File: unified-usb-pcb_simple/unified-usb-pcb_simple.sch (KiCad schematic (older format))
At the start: 11 parts, among them J1 USB_C_Receptacle_USB2.0, J2 USB_Out, U1 SRV05-4

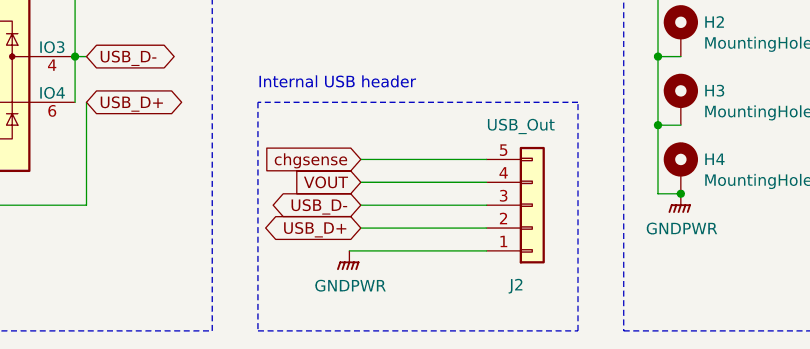
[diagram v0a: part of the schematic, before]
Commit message: added ferrite bead, improved usb track matching
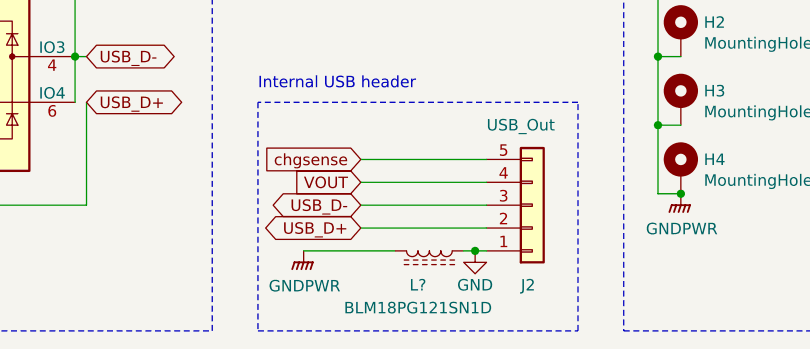
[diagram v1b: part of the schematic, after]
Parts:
- added L?: BLM18PG121SN1D, Inductor_SMD:L_0603_1608Metric, symbol Device:L_Core_Ferrite
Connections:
- net GNDPWR: now also L?.2; no longer J2.1 (Pin_1)
- new net GND: J2.1 (Pin_1), L?.1
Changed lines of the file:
@@
 U 1 1 5E8A3E4C
 P 5350 2300
-F 0 "J2" H 5250 2650 50  0000 L CNN
+F 0 "J2" H 5300 2650 50  0000 L CNN
 F 1 "USB_Out" H 5150 1950 50  0000 L CNN
 F 2 "Connector_JST:JST_SH_SM05B-SRSS-TB_1x05-1MP_P1.00mm_Horizontal" H 5350 2300 50  0001 C CNN
@@
 L power:GNDPWR #PWR03
 U 1 1 5E879D91
-P 4550 2500
-F 0 "#PWR03" H 4550 2300 50  0001 C CNN
-F 1 "GNDPWR" H 4554 2346 50  0000 C CNN
-F 2 "" H 4550 2450 50  0001 C CNN
-F 3 "" H 4550 2450 50  0001 C CNN
-	1    4550 2500
-	1    0    0    -1
-$EndComp
-Wire Wire Line
-	5150 2500 4550 2500
+P 4350 2500
+F 0 "#PWR03" H 4350 2300 50  0001 C CNN
+F 1 "GNDPWR" H 4354 2346 50  0000 C CNN
+F 2 "" H 4350 2450 50  0001 C CNN
+F 3 "" H 4350 2450 50  0001 C CNN
+	1    4350 2500
+	1    0    0    -1
+$EndComp
 Text GLabel 4600 2100 0    50   Input ~ 0
 chgsense
@@
 Wire Wire Line
 	4600 2200 5150 2200
+$Comp
+L Device:L_Core_Ferrite L?
+U 1 1 5E8E3A4F
+P 4900 2500
+F 0 "L?" V 5050 2450 50  0000 C CNN
+F 1 "BLM18PG121SN1D" V 5150 2450 50  0000 C CNN
+F 2 "Inductor_SMD:L_0603_1608Metric" H 4900 2500 50  0001 C CNN
+F 3 "~" H 4900 2500 50  0001 C CNN
+	1    4900 2500
+	0    1    1    0
+$EndComp
+Wire Wire Line
+	5050 2500 5100 2500
+Wire Wire Line
+	4750 2500 4350 2500
+$Comp
+L power:GND #PWR?
+U 1 1 5E8E879D
+P 5100 2500
+F 0 "#PWR?" H 5100 2250 50  0001 C CNN
+F 1 "GND" H 5100 2350 50  0000 C CNN
+F 2 "" H 5100 2500 50  0001 C CNN
+F 3 "" H 5100 2500 50  0001 C CNN
+	1    5100 2500
+	1    0    0    -1
+$EndComp
+Connection ~ 5100 2500
+Wire Wire Line
+	5100 2500 5150 2500
 $EndSCHEMATC

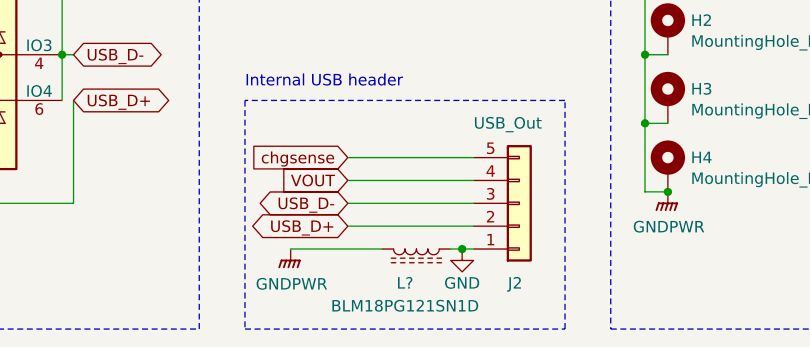
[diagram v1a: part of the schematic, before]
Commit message: added ferrite bead
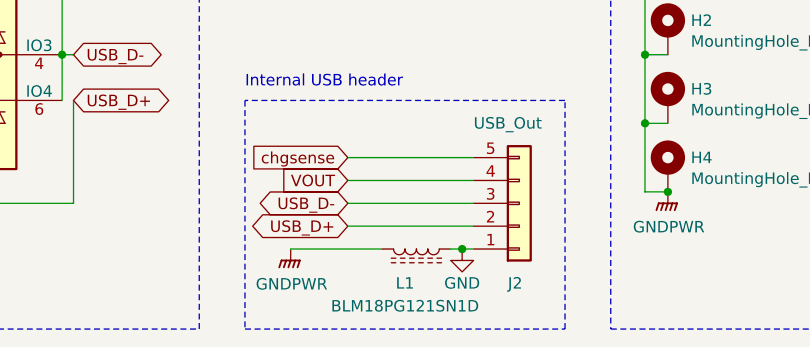
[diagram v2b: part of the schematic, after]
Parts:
- gave numbers to parts that had none: 1
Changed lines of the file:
@@
 	4600 2200 5150 2200
 $Comp
-L Device:L_Core_Ferrite L?
+L Device:L_Core_Ferrite L1
 U 1 1 5E8E3A4F
 P 4900 2500
-F 0 "L?" V 5050 2450 50  0000 C CNN
+F 0 "L1" V 5050 2450 50  0000 C CNN
 F 1 "BLM18PG121SN1D" V 5150 2450 50  0000 C CNN
 F 2 "Inductor_SMD:L_0603_1608Metric" H 4900 2500 50  0001 C CNN
@@
 	4750 2500 4350 2500
 $Comp
-L power:GND #PWR?
+L power:GND #PWR0101
 U 1 1 5E8E879D
 P 5100 2500
-F 0 "#PWR?" H 5100 2250 50  0001 C CNN
+F 0 "#PWR0101" H 5100 2250 50  0001 C CNN
 F 1 "GND" H 5100 2350 50  0000 C CNN
 F 2 "" H 5100 2500 50  0001 C CNN

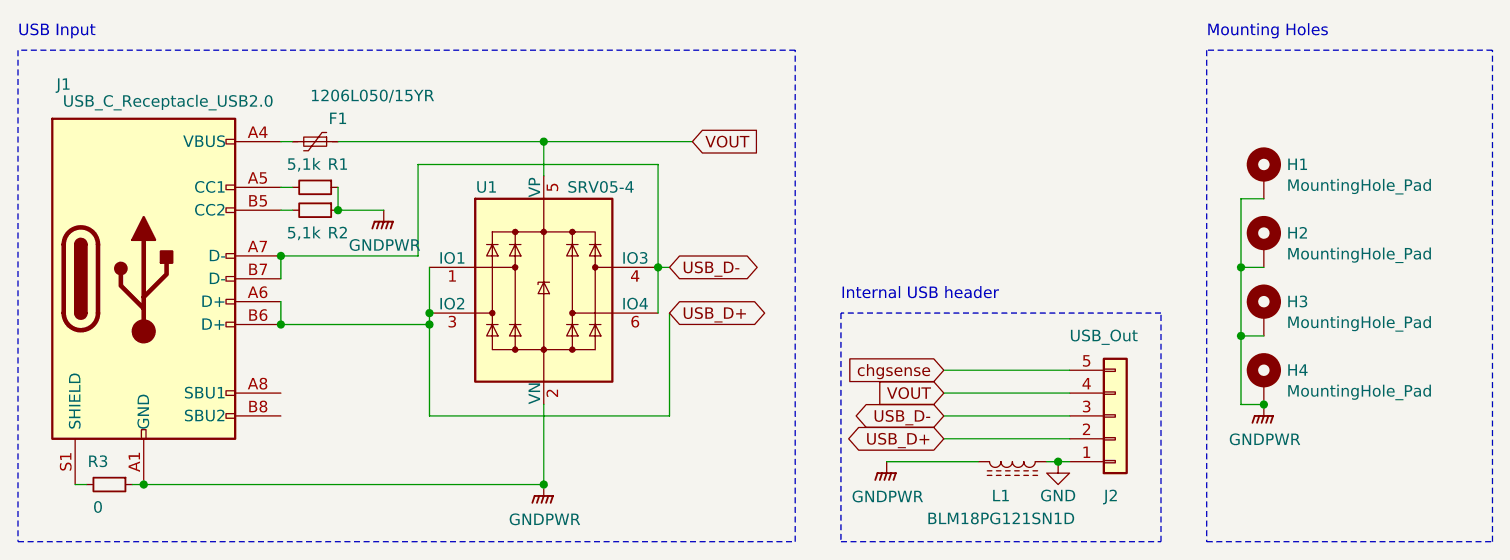
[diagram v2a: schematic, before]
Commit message: created plane for usb-shielding below the connector
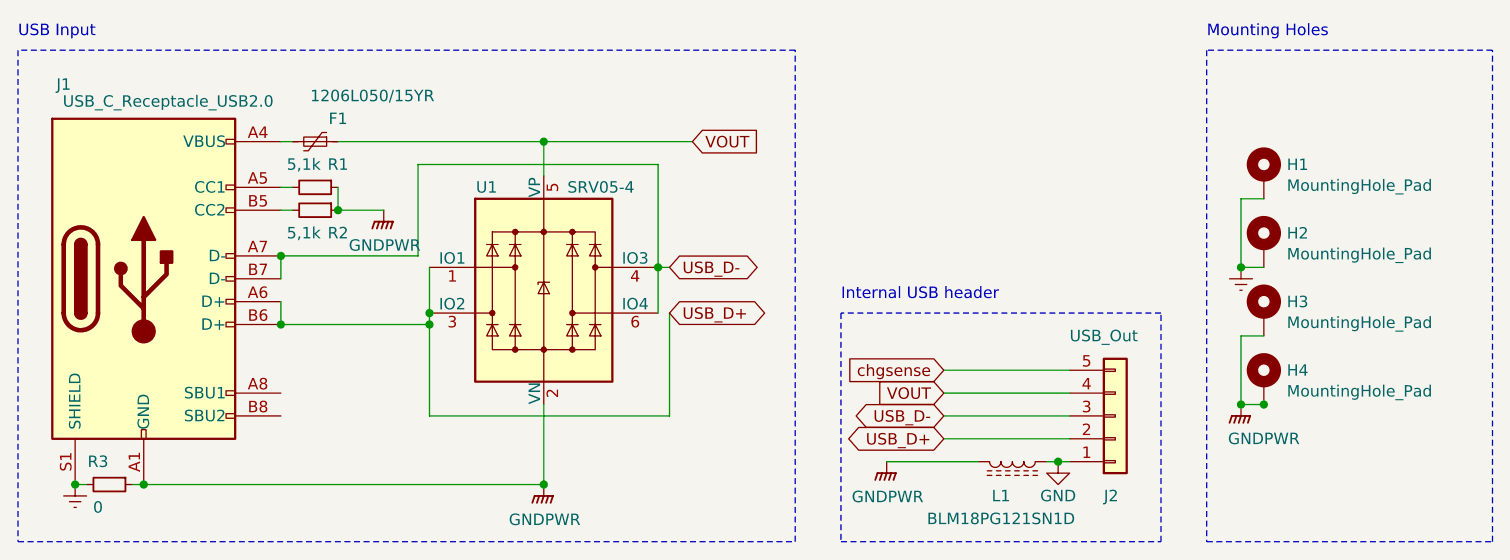
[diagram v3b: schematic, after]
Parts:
- F1: LCSC (none) -> C151162
- H1, H2, H3, H4, J1, J2: LCSC (none) -> /
- L1: LCSC (none) -> C73100
- R1, R2: LCSC (none) -> C23186
- R3: LCSC (none) -> C21189
- U1: LCSC (none) -> C85364
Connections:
- net GNDPWR: no longer H1.1, H2.1
- net Earth: now reaches J1.S1 (SHIELD), R3.2
- net Earth: now also H1.1, H2.1
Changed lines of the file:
@@
 F 2 "Connector_USB:USB_C_Receptacle_HRO_TYPE-C-31-M-12" H 1250 1700 50  0001 C CNN
 F 3 "https://www.usb.org/sites/default/files/documents/usb_type-c.zip" H 1250 1700 50  0001 C CNN
+F 4 "/" H 1100 1700 50  0001 C CNN "LCSC"
 	1    1100 1700
 	1    0    0    -1
@@
 F 2 "Package_TO_SOT_SMD:SOT-23-6" H 3550 1300 50  0001 C CNN
 F 3 "http://www.onsemi.com/pub/Collateral/SRV05-4-D.PDF" H 2850 1750 50  0001 C CNN
+F 4 "C85364" H 2850 1750 50  0001 C CNN "LCSC"
 	1    2850 1750
 	1    0    0    -1
@@
 F 2 "Resistor_SMD:R_0603_1608Metric" H 950 2600 50  0001 C CNN
 F 3 "~" H 950 2600 50  0001 C CNN
+F 4 "C21189" H 950 2600 50  0001 C CNN "LCSC"
 	1    950  2600
 	0    1    1    0
@@
 F 2 "Resistor_SMD:R_0603_1608Metric" H 1850 1300 50  0001 C CNN
 F 3 "~" H 1850 1300 50  0001 C CNN
+F 4 "C23186" H 1850 1300 50  0001 C CNN "LCSC"
 	1    1850 1300
 	0    1    1    0
@@
 F 2 "Resistor_SMD:R_0603_1608Metric" H 1850 1400 50  0001 C CNN
 F 3 "~" H 1850 1400 50  0001 C CNN
+F 4 "C23186" H 1850 1400 50  0001 C CNN "LCSC"
 	1    1850 1400
 	0    1    1    0
@@
 F 2 "Connector_JST:JST_SH_SM05B-SRSS-TB_1x05-1MP_P1.00mm_Horizontal" H 5350 2300 50  0001 C CNN
 F 3 "~" H 5350 2300 50  0001 C CNN
+F 4 "/" H 5350 2300 50  0001 C CNN "LCSC"
 	1    5350 2300
 	1    0    0    1
@@
 F 2 "Fuse:Fuse_1206_3216Metric" H 1900 900 50  0001 L CNN
 F 3 "https://datasheet.lcsc.com/szlcsc/1810252220_Fuzetec-Tech-FSMD050-1206-R_C220147.pdf" H 1850 1100 50  0001 C CNN
+F 4 "C151162" H 1850 1100 50  0001 C CNN "LCSC"
 	1    1850 1100
 	0    1    1    0
@@
 F 2 "MountingHole:MountingHole_2.7mm_M2.5_DIN965_Pad" H 6000 1250 50  0001 C CNN
 F 3 "~" H 6000 1250 50  0001 C CNN
+F 4 "/" H 6000 1250 50  0001 C CNN "LCSC"
 	1    6000 1250
 	1    0    0    -1
@@
 F 2 "MountingHole:MountingHole_2.7mm_M2.5_DIN965_Pad" H 6000 1550 50  0001 C CNN
 F 3 "~" H 6000 1550 50  0001 C CNN
+F 4 "/" H 6000 1550 50  0001 C CNN "LCSC"
 	1    6000 1550
 	1    0    0    -1
@@
 F 2 "MountingHole:MountingHole_2.7mm_M2.5_DIN965_Pad" H 6000 1850 50  0001 C CNN
 F 3 "~" H 6000 1850 50  0001 C CNN
+F 4 "/" H 6000 1850 50  0001 C CNN "LCSC"
 	1    6000 1850
 	1    0    0    -1
@@
 F 2 "MountingHole:MountingHole_2.7mm_M2.5_DIN965_Pad" H 6000 2150 50  0001 C CNN
 F 3 "~" H 6000 2150 50  0001 C CNN
+F 4 "/" H 6000 2150 50  0001 C CNN "LCSC"
 	1    6000 2150
 	1    0    0    -1
@@
 	5900 1650 6000 1650
 Wire Wire Line
-	5900 1650 5900 1950
-Wire Wire Line
 	5900 1950 6000 1950
-Connection ~ 5900 1650
 Wire Wire Line
 	5900 1950 5900 2250
 Wire Wire Line
 	5900 2250 6000 2250
-Connection ~ 5900 1950
 $Comp
 L power:GNDPWR #PWR02
 U 1 1 5E8EB80F
-P 6000 2250
-F 0 "#PWR02" H 6000 2050 50  0001 C CNN
-F 1 "GNDPWR" H 6004 2096 50  0000 C CNN
-F 2 "" H 6000 2200 50  0001 C CNN
-F 3 "" H 6000 2200 50  0001 C CNN
-	1    6000 2250
+P 5900 2250
+F 0 "#PWR02" H 5900 2050 50  0001 C CNN
+F 1 "GNDPWR" H 6000 2100 50  0000 C CNN
+F 2 "" H 5900 2200 50  0001 C CNN
+F 3 "" H 5900 2200 50  0001 C CNN
+	1    5900 2250
 	1    0    0    -1
 $EndComp
@@
 F 2 "Inductor_SMD:L_0603_1608Metric" H 4900 2500 50  0001 C CNN
 F 3 "~" H 4900 2500 50  0001 C CNN
+F 4 "C73100" H 4900 2500 50  0001 C CNN "LCSC"
 	1    4900 2500
 	0    1    1    0
@@
 Wire Wire Line
 	5100 2500 5150 2500
+$Comp
+L power:Earth #PWR?
+U 1 1 5EBED781
+P 800 2600
+F 0 "#PWR?" H 800 2350 50  0001 C CNN
+F 1 "Earth" H 800 2450 50  0001 C CNN
+F 2 "" H 800 2600 50  0001 C CNN
+F 3 "~" H 800 2600 50  0001 C CNN
+	1    800  2600
+	1    0    0    -1
+$EndComp
+Connection ~ 800  2600
+$Comp
+L power:Earth #PWR?
+U 1 1 5EBEE999
+P 5900 1650
+F 0 "#PWR?" H 5900 1400 50  0001 C CNN
+F 1 "Earth" H 5900 1500 50  0001 C CNN
+F 2 "" H 5900 1650 50  0001 C CNN
+F 3 "~" H 5900 1650 50  0001 C CNN
+	1    5900 1650
+	1    0    0    -1
+$EndComp
+Connection ~ 5900 1650
+Connection ~ 5900 2250
 $EndSCHEMATC

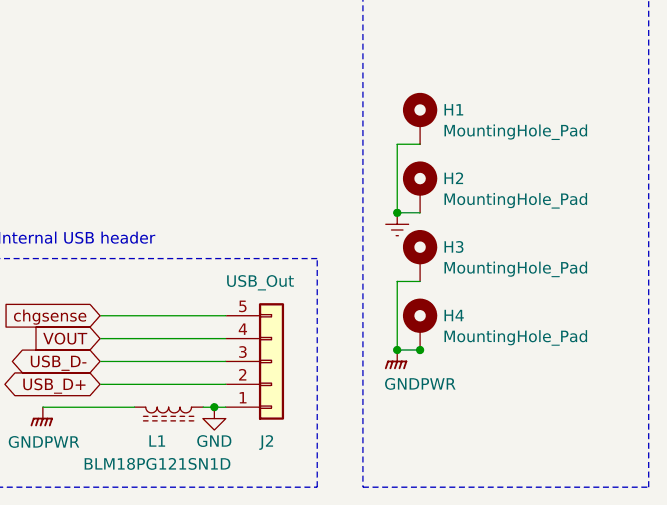
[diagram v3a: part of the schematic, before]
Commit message: resized shield plane
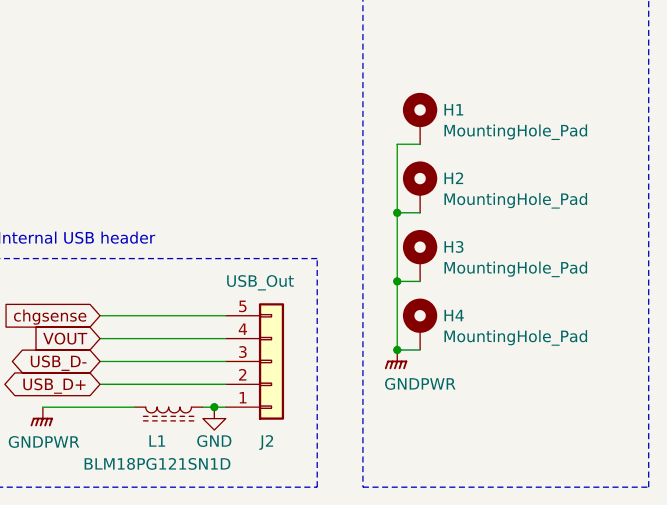
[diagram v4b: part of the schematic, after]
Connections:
- net Earth: no longer H1.1, H2.1
- net GNDPWR: now also H1.1, H2.1
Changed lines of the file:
@@
 	1    0    0    -1
 $EndComp
-Connection ~ 6000 2250
 Wire Notes Line style solid
 	5750 700  5750 2850
@@
 	5100 2500 5150 2500
 $Comp
-L power:Earth #PWR?
+L power:Earth #PWR0102
 U 1 1 5EBED781
 P 800 2600
-F 0 "#PWR?" H 800 2350 50  0001 C CNN
+F 0 "#PWR0102" H 800 2350 50  0001 C CNN
 F 1 "Earth" H 800 2450 50  0001 C CNN
 F 2 "" H 800 2600 50  0001 C CNN
@@
 $EndComp
 Connection ~ 800  2600
-$Comp
-L power:Earth #PWR?
-U 1 1 5EBEE999
-P 5900 1650
-F 0 "#PWR?" H 5900 1400 50  0001 C CNN
-F 1 "Earth" H 5900 1500 50  0001 C CNN
-F 2 "" H 5900 1650 50  0001 C CNN
-F 3 "~" H 5900 1650 50  0001 C CNN
-	1    5900 1650
-	1    0    0    -1
-$EndComp
+Connection ~ 5900 2250
+Wire Wire Line
+	5900 1650 5900 1950
 Connection ~ 5900 1650
-Connection ~ 5900 2250
+Connection ~ 5900 1950
 $EndSCHEMATC

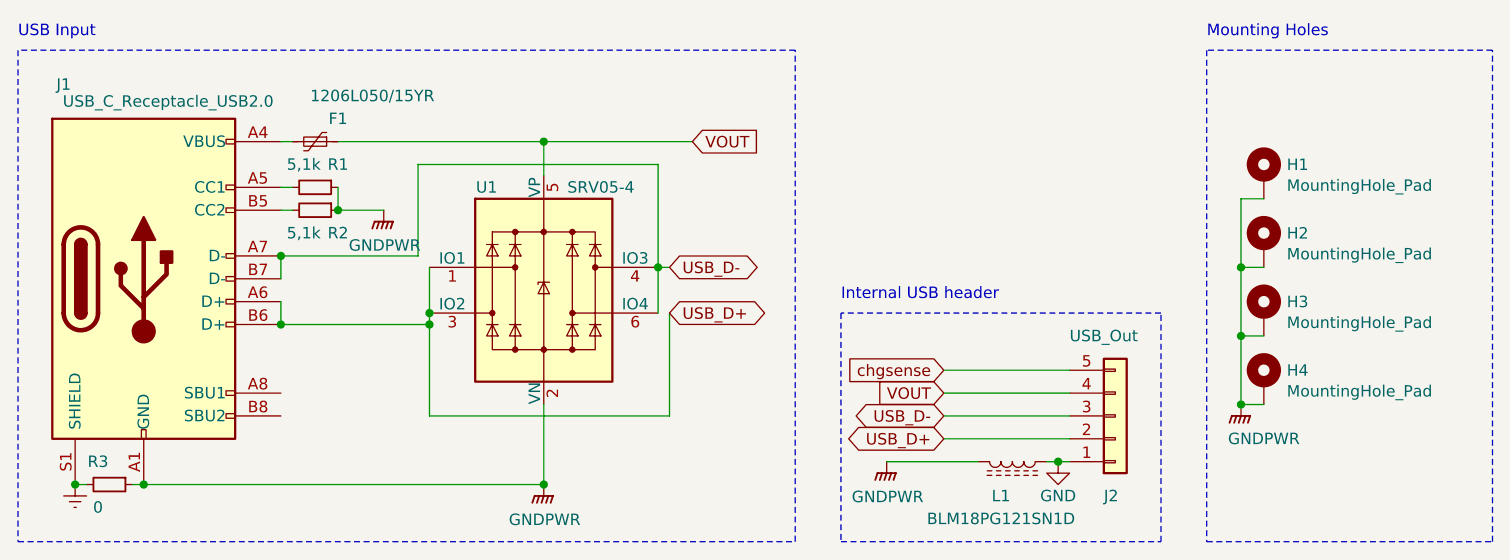
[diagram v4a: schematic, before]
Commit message: added manufacturing files
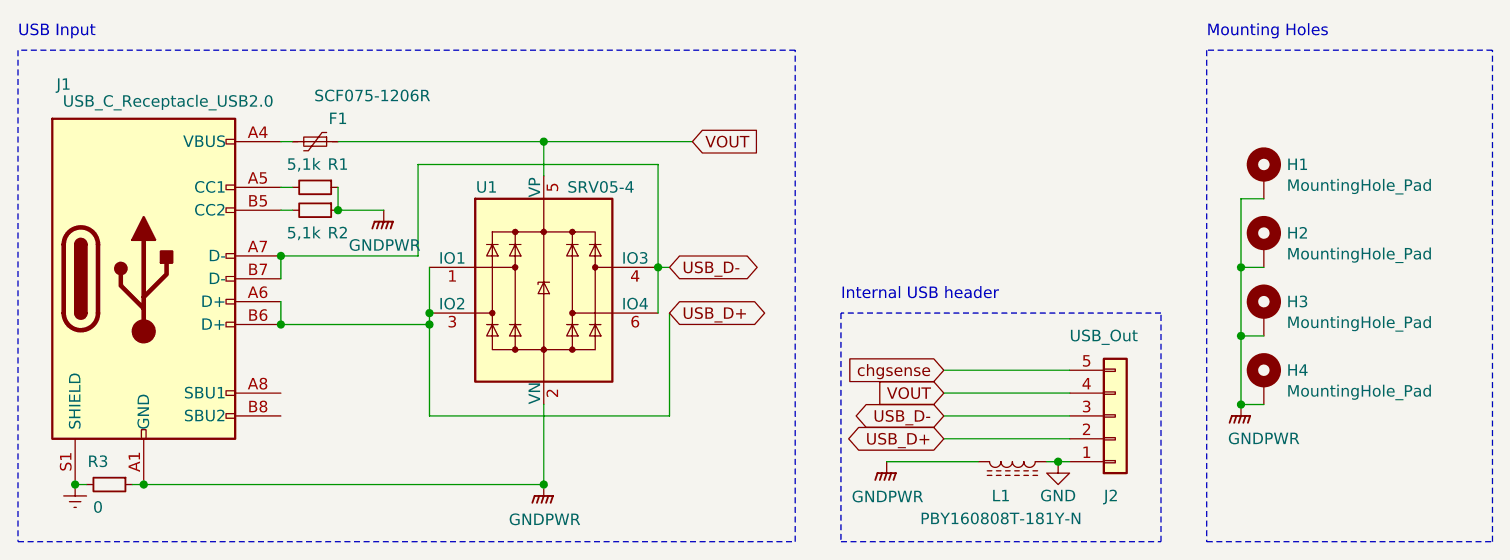
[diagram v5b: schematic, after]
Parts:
- F1: value 1206L050/15YR -> SCF075-1206R; LCSC C151162 -> C183290
- L1: value BLM18PG121SN1D -> PBY160808T-181Y-N; LCSC C73100 -> C114288
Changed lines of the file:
@@
 P 1850 1100
 F 0 "F1" V 1750 1200 50  0000 C CNN
-F 1 "1206L050/15YR" V 1650 1350 50  0000 C CNN
+F 1 "SCF075-1206R" V 1650 1350 50  0000 C CNN
 F 2 "Fuse:Fuse_1206_3216Metric" H 1900 900 50  0001 L CNN
-F 3 "https://datasheet.lcsc.com/szlcsc/1810252220_Fuzetec-Tech-FSMD050-1206-R_C220147.pdf" H 1850 1100 50  0001 C CNN
-F 4 "C151162" H 1850 1100 50  0001 C CNN "LCSC"
+F 3 "https://datasheet.lcsc.com/szlcsc/SOCAY-Elec-SCF075-1206R_C183290.pdf" H 1850 1100 50  0001 C CNN
+F 4 "C183290" H 1850 1100 50  0001 C CNN "LCSC"
 	1    1850 1100
 	0    1    1    0
@@
 P 4900 2500
 F 0 "L1" V 5050 2450 50  0000 C CNN
-F 1 "BLM18PG121SN1D" V 5150 2450 50  0000 C CNN
+F 1 "PBY160808T-181Y-N" V 5150 2450 50  0000 C CNN
 F 2 "Inductor_SMD:L_0603_1608Metric" H 4900 2500 50  0001 C CNN
 F 3 "~" H 4900 2500 50  0001 C CNN
-F 4 "C73100" H 4900 2500 50  0001 C CNN "LCSC"
+F 4 " C114288" H 4900 2500 50  0001 C CNN "LCSC"
 	1    4900 2500
 	0    1    1    0
